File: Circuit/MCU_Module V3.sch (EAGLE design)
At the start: 44 parts, among them IC1 75176BD, Q1 8MHZ, T1 BC848, T2 BC848

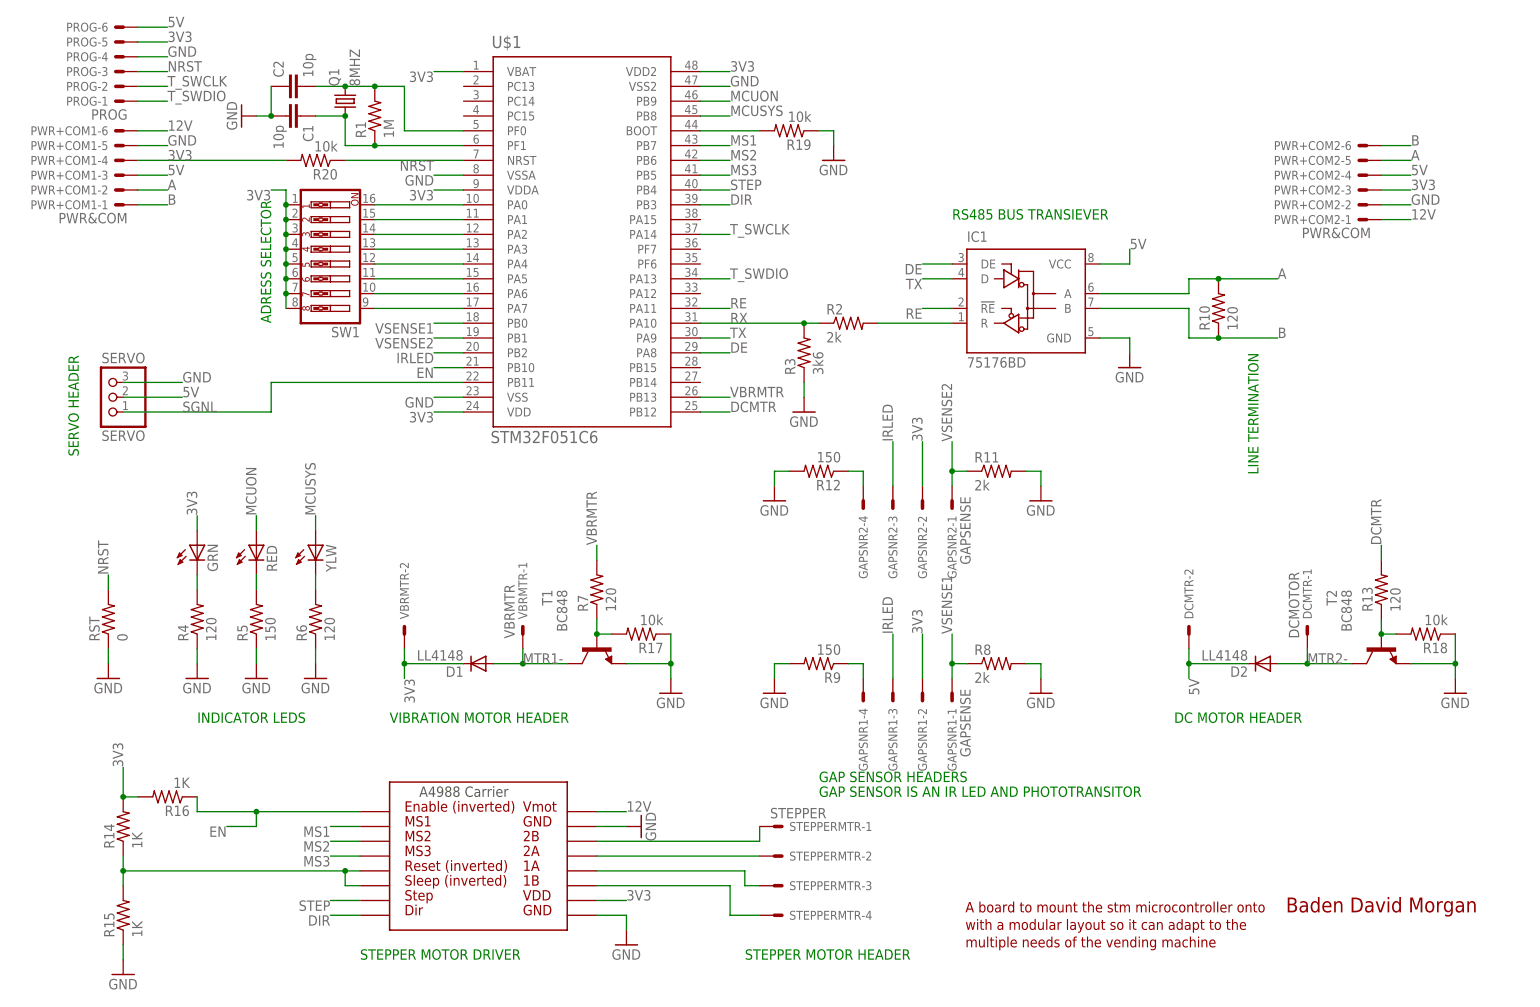
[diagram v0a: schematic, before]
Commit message: redid layout and updated document
updated the document and redid the layout to improve layout and added
more initilizaton to the document
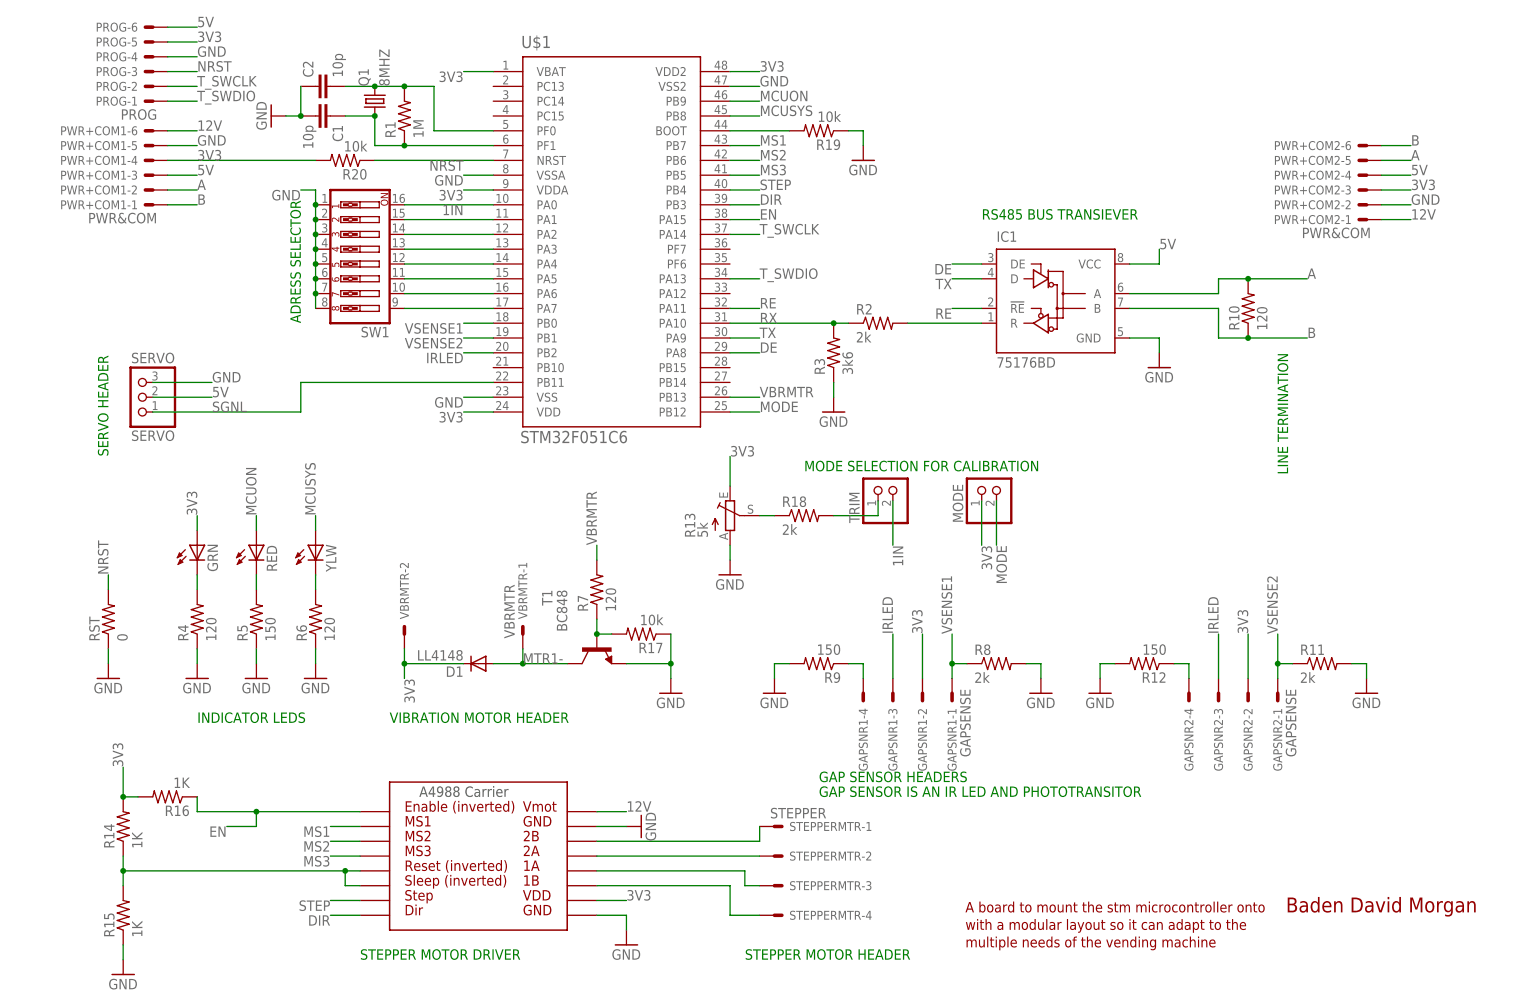
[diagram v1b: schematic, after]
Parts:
- removed D2: LL4148, diode:PMLL4150
- removed DCMTR: DCMOTOR, con-molex:22-27-2021-02
- removed T2: BC848, transistor:BC848
- added MODE, TRIM: (no value), pinhead:PINHD-1X2
- R13: value 120 -> 5k; device rcl:R-US_R0805 -> pot:TRIM_EU-B25P
- R18: value 10k -> 2k; device rcl:R-US_R0805 -> resistor:R-US_R0805
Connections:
- net N$13 renamed 8IN
- removed net DCMTR: R13.2, U$1.PB12
- removed net MTR2-: D2.A, DCMTR-1.S, T2.C
- removed net N$3: SW1.16, U$1.PA0
- removed net N$4: R13.1, R18.2, T2.B
- new net 1IN: SW1.16, TRIM.2, U$1.PA0
- new net MODE: MODE.2, U$1.PB12
- new net N$13: R13.S, R18.1
- new net N$23: R18.2, TRIM.1
- net 3V3: now also MODE.1, R13.E; no longer SW1.1, SW1.2, SW1.3, SW1.4, SW1.5, SW1.6, SW1.7, SW1.8
- net 5V: no longer D2.C, DCMTR-2.S
- net EN: now also U$1.PA15; no longer U$1.PB10
- net GND: now also R13.A, SW1.1, SW1.2, SW1.3, SW1.4, SW1.5, SW1.6, SW1.7, SW1.8; no longer R18.1, T2.E
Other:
- note added: "MODE SELECTION FOR CALIBRATION"
- note removed: "DC MOTOR HEADER"
- moved on the sheet: C1, C2, GAPSNR2-1, GAPSNR2-2, GAPSNR2-3, GAPSNR2-4, IC1, PROG-1, PROG-2, PROG-3, PROG-4, PROG-5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
